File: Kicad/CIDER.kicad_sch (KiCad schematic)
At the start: 0 parts

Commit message: PCB: Fixups
* Tweak KEL connector hole sizes
* Fixup MT48LC8M16A2P - Had copied this from the 16M16 part and forgot to make A12 an NC
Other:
- company: (none) -> Matt Harlum
- title: (none) -> CIDER
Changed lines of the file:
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@@
 (kicad_sch (version 20211123) (generator eeschema)
   (paper "A4")
+  (title_block
+    (title "CIDER")
+    (company "Matt Harlum")
+  )
   (junction (at 147.32 126.365) (diameter 0) (color 0 0 0 0)
   )
@@
       (reference "#PWR059") (unit 1) (value "GND") (footprint "")
     )
+    (path "/b306c586-f0fb-4048-9e1c-70c4b12a13fa/ebe895d5-8243-4384-af5b-a2d715f74b0e"
+      (reference "#PWR060") (unit 1) (value "VCC") (footprint "")
+    )
+    (path "/b306c586-f0fb-4048-9e1c-70c4b12a13fa/95d31eed-361c-43ce-9f04-8fd42c9b94c6"
+      (reference "#PWR061") (unit 1) (value "GND") (footprint "")
+    )
     (path "/b306c586-f0fb-4048-9e1c-70c4b12a13fa/e000336a-200f-46b9-a82c-1a20eb3f6b2b"
       (reference "C1") (unit 1) (value "0.1u") (footprint "Capacitor_SMD:C_0603_1608Metric")
@@
       (reference "C26") (unit 1) (value "0.1u") (footprint "Capacitor_SMD:C_0603_1608Metric")
     )
+    (path "/b306c586-f0fb-4048-9e1c-70c4b12a13fa/9314d797-b935-4e90-920d-c3b504732092"
+      (reference "C27") (unit 1) (value "47u") (footprint "Capacitor_Tantalum_SMD:CP_EIA-3216-18_Kemet-A")
+    )
     (path "/b306c586-f0fb-4048-9e1c-70c4b12a13fa/c947839d-6612-4454-8256-bf64cecbe088"
       (reference "CN1") (unit 1) (value "CDTV-DIAG") (footprint "KEL-8800-080-170SF:KEL-8800-080-170S")
@@
     )
     (path "/b306c586-f0fb-4048-9e1c-70c4b12a13fa/689c27d0-1654-4831-a4cf-f0ff1f3a33e5"
-      (reference "RN1") (unit 1) (value "R_Pack04") (footprint "Resistor_SMD:R_Array_Convex_4x0603")
+      (reference "RN1") (unit 1) (value "10K") (footprint "Resistor_SMD:R_Array_Convex_4x0603")
     )
     (path "/630b208b-10ae-4511-a2aa-10492c9d744e/b54956b9-e455-4d14-a564-3a7bd4c7a606"
-      (reference "RN2") (unit 1) (value "R_Pack04") (footprint "Resistor_SMD:R_Array_Convex_4x0603")
+      (reference "RN2") (unit 1) (value "22") (footprint "Resistor_SMD:R_Array_Convex_4x0603")
     )
     (path "/630b208b-10ae-4511-a2aa-10492c9d744e/493fecd9-d3f5-4099-abf0-9ac9312fac38"
-      (reference "RN3") (unit 1) (value "R_Pack04") (footprint "Resistor_SMD:R_Array_Convex_4x0603")
+      (reference "RN3") (unit 1) (value "22") (footprint "Resistor_SMD:R_Array_Convex_4x0603")
     )
     (path "/630b208b-10ae-4511-a2aa-10492c9d744e/1a118d6d-4f6c-4fe2-86f2-dc6f8678016d"
-      (reference "RN4") (unit 1) (value "R_Pack04") (footprint "Resistor_SMD:R_Array_Convex_4x0603")
+      (reference "RN4") (unit 1) (value "22") (footprint "Resistor_SMD:R_Array_Convex_4x0603")
     )
     (path "/630b208b-10ae-4511-a2aa-10492c9d744e/622a6d78-7f2a-4d0b-9a66-0a395de1429b"
-      (reference "RN5") (unit 1) (value "R_Pack04") (footprint "Resistor_SMD:R_Array_Convex_4x0603")
+      (reference "RN5") (unit 1) (value "22") (footprint "Resistor_SMD:R_Array_Convex_4x0603")
     )
     (path "/b306c586-f0fb-4048-9e1c-70c4b12a13fa/c64e7f71-5f52-4706-9302-2f8168b83a4d"

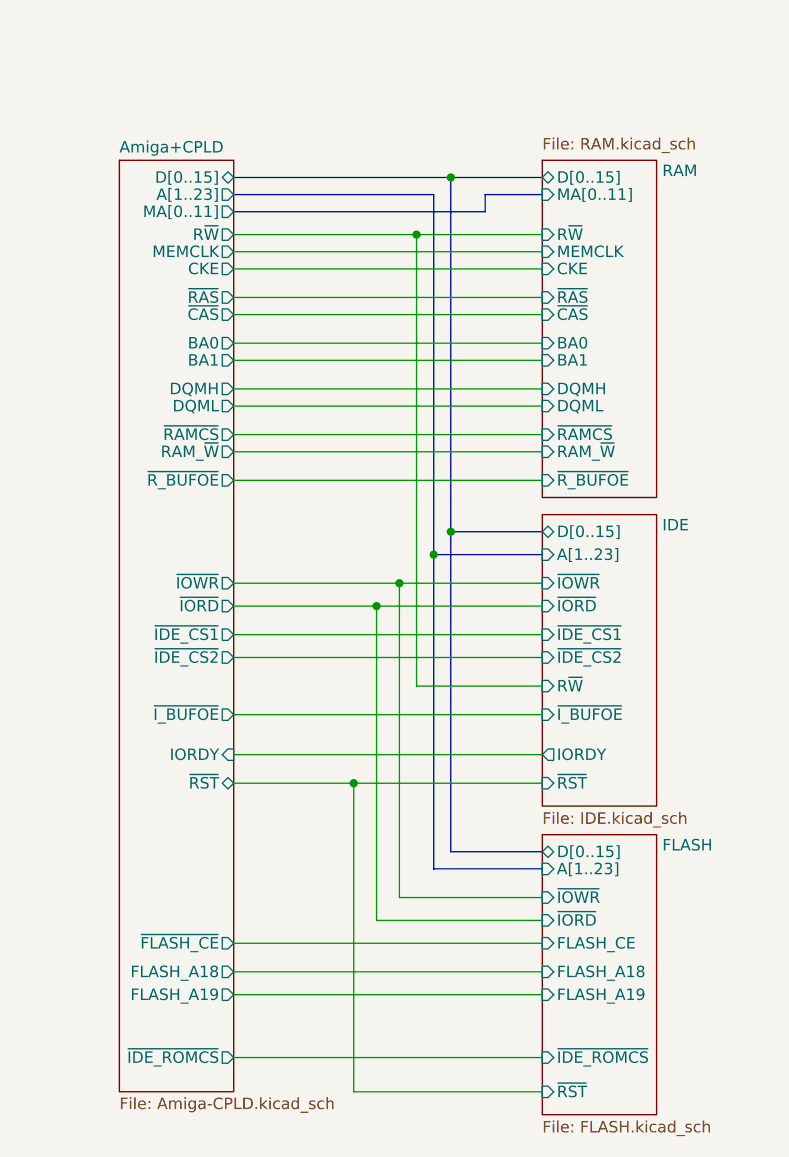
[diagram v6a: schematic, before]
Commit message: Rev-A1: Buffer A500/Bank Sel switches
Added inline resistors to these two and buffer them via U5
In Proto A it was found that operating the switches would cause latch-up and destroy the CPLD
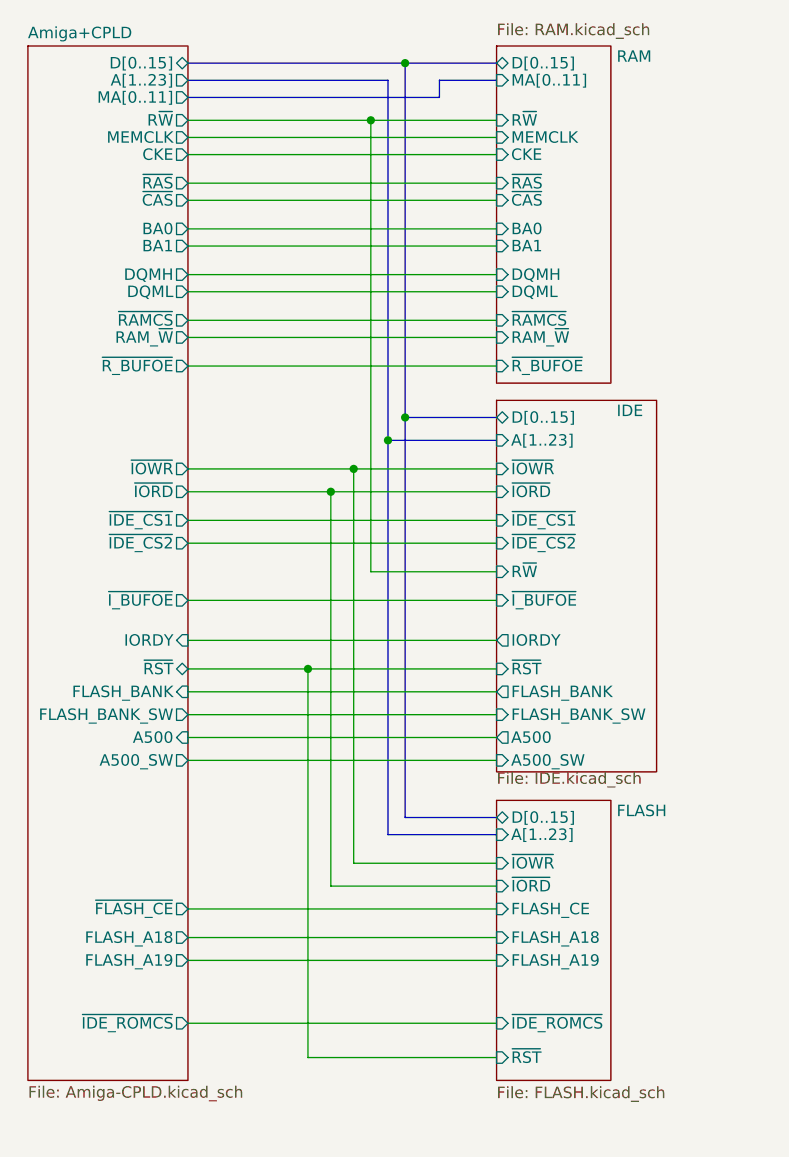
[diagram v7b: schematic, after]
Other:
- sheet Amiga+CPLD ports: added A500, A500_SW, FLASH_BANK, FLASH_BANK_SW; removed none
- sheet IDE ports: added A500, A500_SW, FLASH_BANK, FLASH_BANK_SW; removed none
